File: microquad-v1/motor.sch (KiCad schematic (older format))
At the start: 5 parts, among them M6 Motor_DC, Q6 Q_NMOS_DGS

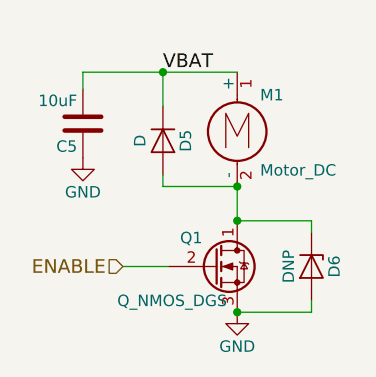
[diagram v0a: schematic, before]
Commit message: Added layout for transistor
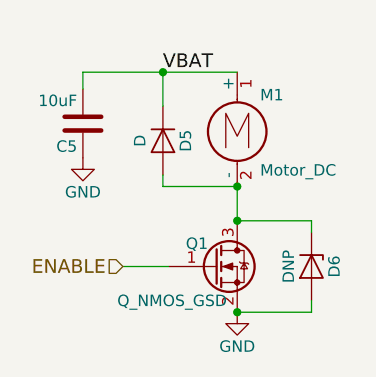
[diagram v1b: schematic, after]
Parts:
- removed Q6: Q_NMOS_DGS, symbol Q_NMOS_DGS
- added Q1: Q_NMOS_GSD, TO_SOT_Packages_SMD:SOT-23, symbol Q_NMOS_GSD
- C10: footprint (none) -> Capacitors_SMD:C_0805
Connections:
- net ENABLE: now also Q1.1 (G)
- net GND: now also Q1.2 (S)
- net at D5.2 (A), D6.1 (K), M6.2 (-): now also Q1.3 (D)
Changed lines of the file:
@@
 $EndDescr
 $Comp
-L Q_NMOS_DGS Q6
-U 1 1 59F7E923
-P 4875 3200
-AR Path="/59F7FFA4/59F7E923" Ref="Q6"  Part="1"
-AR Path="/59F7E793/59F7E923" Ref="Q1"  Part="1"
-AR Path="/59F7F6E8/59F7E923" Ref="Q2"  Part="1"
-AR Path="/59F7FC5E/59F7E923" Ref="Q3"  Part="1"
-AR Path="/59F7FC61/59F7E923" Ref="Q4"  Part="1"
-AR Path="/59F7FFA1/59F7E923" Ref="Q5"  Part="1"
-F 0 "Q1" H 4725 3325 50  0000 L CNN
-F 1 "Q_NMOS_DGS" H 4450 3050 50  0000 L CNN
-F 2 "" H 5075 3300 50  0001 C CNN
-F 3 "" H 4875 3200 50  0001 C CNN
-	1    4875 3200
-	1    0    0    -1
-$EndComp
-$Comp
-L GND #PWR57
+L GND #PWR058
 U 1 1 59F7E92A
 P 4975 3400
-AR Path="/59F7FFA4/59F7E92A" Ref="#PWR57"  Part="1"
-AR Path="/59F7E793/59F7E92A" Ref="#PWR47"  Part="1"
-AR Path="/59F7F6E8/59F7E92A" Ref="#PWR49"  Part="1"
-AR Path="/59F7FC5E/59F7E92A" Ref="#PWR51"  Part="1"
-AR Path="/59F7FC61/59F7E92A" Ref="#PWR53"  Part="1"
-AR Path="/59F7FFA1/59F7E92A" Ref="#PWR55"  Part="1"
-F 0 "#PWR47" H 4975 3150 50  0001 C CNN
+AR Path="/59F7FFA4/59F7E92A" Ref="#PWR058"  Part="1"
+AR Path="/59F7E793/59F7E92A" Ref="#PWR048"  Part="1"
+AR Path="/59F7F6E8/59F7E92A" Ref="#PWR050"  Part="1"
+AR Path="/59F7FC5E/59F7E92A" Ref="#PWR052"  Part="1"
+AR Path="/59F7FC61/59F7E92A" Ref="#PWR054"  Part="1"
+AR Path="/59F7FFA1/59F7E92A" Ref="#PWR056"  Part="1"
+F 0 "#PWR048" H 4975 3150 50  0001 C CNN
 F 1 "GND" H 4975 3250 50  0000 C CNN
 F 2 "" H 4975 3400 50  0001 C CNN
@@
 F 0 "C5" H 4325 2675 50  0000 L CNN
 F 1 "10uF" H 4325 2475 50  0000 L CNN
-F 2 "" H 4338 2425 50  0001 C CNN
+F 2 "Capacitors_SMD:C_0805" H 4338 2425 50  0001 C CNN
 F 3 "" H 4300 2575 50  0001 C CNN
 	1    4300 2575
@@
 Connection ~ 4650 2350
 $Comp
-L GND #PWR56
+L GND #PWR059
 U 1 1 59F80F77
 P 4300 2725
-AR Path="/59F7FFA4/59F80F77" Ref="#PWR56"  Part="1"
-AR Path="/59F7E793/59F80F77" Ref="#PWR46"  Part="1"
-AR Path="/59F7F6E8/59F80F77" Ref="#PWR48"  Part="1"
-AR Path="/59F7FC5E/59F80F77" Ref="#PWR50"  Part="1"
-AR Path="/59F7FC61/59F80F77" Ref="#PWR52"  Part="1"
-AR Path="/59F7FFA1/59F80F77" Ref="#PWR54"  Part="1"
-F 0 "#PWR46" H 4300 2475 50  0001 C CNN
+AR Path="/59F7FFA4/59F80F77" Ref="#PWR059"  Part="1"
+AR Path="/59F7E793/59F80F77" Ref="#PWR049"  Part="1"
+AR Path="/59F7F6E8/59F80F77" Ref="#PWR051"  Part="1"
+AR Path="/59F7FC5E/59F80F77" Ref="#PWR053"  Part="1"
+AR Path="/59F7FC61/59F80F77" Ref="#PWR055"  Part="1"
+AR Path="/59F7FFA1/59F80F77" Ref="#PWR057"  Part="1"
+F 0 "#PWR049" H 4300 2475 50  0001 C CNN
 F 1 "GND" H 4300 2575 50  0000 C CNN
 F 2 "" H 4300 2725 50  0001 C CNN
@@
 Connection ~ 4975 3000
 Connection ~ 4975 3400
+$Comp
+L Q_NMOS_GSD Q1
+U 1 1 59F918D5
+P 4875 3200
+AR Path="/59F7E793/59F918D5" Ref="Q1"  Part="1"
+AR Path="/59F7F6E8/59F918D5" Ref="Q2"  Part="1"
+AR Path="/59F7FC5E/59F918D5" Ref="Q3"  Part="1"
+AR Path="/59F7FC61/59F918D5" Ref="Q4"  Part="1"
+AR Path="/59F7FFA1/59F918D5" Ref="Q5"  Part="1"
+AR Path="/59F7FFA4/59F918D5" Ref="Q6"  Part="1"
+F 0 "Q1" H 4750 3300 50  0000 L CNN
+F 1 "Q_NMOS_GSD" H 4450 3050 50  0000 L CNN
+F 2 "TO_SOT_Packages_SMD:SOT-23" H 5075 3300 50  0001 C CNN
+F 3 "" H 4875 3200 50  0001 C CNN
+	1    4875 3200
+	1    0    0    -1
+$EndComp
 $EndSCHEMATC

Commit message: Finished footprint work 10/31
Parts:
- M6: footprint (none) -> motor:quad_motor_v1
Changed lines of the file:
@@
 AR Path="/59F7FC61/59F7E931" Ref="M4"  Part="1"
 AR Path="/59F7FFA1/59F7E931" Ref="M5"  Part="1"
-F 0 "M1" H 5075 2650 50  0000 L CNN
+F 0 "M6" H 5075 2650 50  0000 L CNN
 F 1 "Motor_DC" H 5075 2350 50  0000 L TNN
-F 2 "" H 4975 2460 50  0001 C CNN
+F 2 "motor:quad_motor_v1" H 4975 2460 50  0001 C CNN
 F 3 "" H 4975 2460 50  0001 C CNN
 	1    4975 2550
@@
 AR Path="/59F7FC61/59F7E93C" Ref="D11"  Part="1"
 AR Path="/59F7FFA1/59F7E93C" Ref="D13"  Part="1"
-F 0 "D5" H 4650 2750 50  0000 C CNN
+F 0 "D15" H 4650 2750 50  0000 C CNN
 F 1 "D" H 4650 2550 50  0000 C CNN
 F 2 "" H 4650 2650 50  0001 C CNN
@@
 AR Path="/59F7FC61/59F7E943" Ref="D12"  Part="1"
 AR Path="/59F7FFA1/59F7E943" Ref="D14"  Part="1"
-F 0 "D6" H 5300 3300 50  0000 C CNN
+F 0 "D16" H 5300 3300 50  0000 C CNN
 F 1 "DNP" H 5300 3100 50  0000 C CNN
 F 2 "" H 5300 3200 50  0001 C CNN
@@
 AR Path="/59F7FC61/59F80E77" Ref="C8"  Part="1"
 AR Path="/59F7FFA1/59F80E77" Ref="C9"  Part="1"
-F 0 "C5" H 4325 2675 50  0000 L CNN
+F 0 "C10" H 4325 2675 50  0000 L CNN
 F 1 "10uF" H 4325 2475 50  0000 L CNN
 F 2 "Capacitors_SMD:C_0805" H 4338 2425 50  0001 C CNN
@@
 AR Path="/59F7FFA1/59F918D5" Ref="Q5"  Part="1"
 AR Path="/59F7FFA4/59F918D5" Ref="Q6"  Part="1"
-F 0 "Q1" H 4750 3300 50  0000 L CNN
+F 0 "Q6" H 4750 3300 50  0000 L CNN
 F 1 "Q_NMOS_GSD" H 4450 3050 50  0000 L CNN
 F 2 "TO_SOT_Packages_SMD:SOT-23" H 5075 3300 50  0001 C CNN

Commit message: Finished in-class work 10/2
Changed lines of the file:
@@
 AR Path="/59F7FC61/59F7E92A" Ref="#PWR054"  Part="1"
 AR Path="/59F7FFA1/59F7E92A" Ref="#PWR056"  Part="1"
-F 0 "#PWR058" H 4975 3150 50  0001 C CNN
+F 0 "#PWR048" H 4975 3150 50  0001 C CNN
 F 1 "GND" H 4975 3250 50  0000 C CNN
 F 2 "" H 4975 3400 50  0001 C CNN
@@
 AR Path="/59F7FC61/59F7E931" Ref="M4"  Part="1"
 AR Path="/59F7FFA1/59F7E931" Ref="M5"  Part="1"
-F 0 "M6" H 5075 2650 50  0000 L CNN
+F 0 "M1" H 5075 2650 50  0000 L CNN
 F 1 "Motor_DC" H 5075 2350 50  0000 L TNN
 F 2 "motor:quad_motor_v1" H 4975 2460 50  0001 C CNN
@@
 AR Path="/59F7FC61/59F7E93C" Ref="D11"  Part="1"
 AR Path="/59F7FFA1/59F7E93C" Ref="D13"  Part="1"
-F 0 "D15" H 4650 2750 50  0000 C CNN
+F 0 "D5" H 4650 2750 50  0000 C CNN
 F 1 "D" H 4650 2550 50  0000 C CNN
 F 2 "" H 4650 2650 50  0001 C CNN
@@
 AR Path="/59F7FC61/59F7E943" Ref="D12"  Part="1"
 AR Path="/59F7FFA1/59F7E943" Ref="D14"  Part="1"
-F 0 "D16" H 5300 3300 50  0000 C CNN
+F 0 "D6" H 5300 3300 50  0000 C CNN
 F 1 "DNP" H 5300 3100 50  0000 C CNN
 F 2 "" H 5300 3200 50  0001 C CNN
@@
 AR Path="/59F7FC61/59F80E77" Ref="C8"  Part="1"
 AR Path="/59F7FFA1/59F80E77" Ref="C9"  Part="1"
-F 0 "C10" H 4325 2675 50  0000 L CNN
+F 0 "C5" H 4325 2675 50  0000 L CNN
 F 1 "10uF" H 4325 2475 50  0000 L CNN
 F 2 "Capacitors_SMD:C_0805" H 4338 2425 50  0001 C CNN
@@
 AR Path="/59F7FC61/59F80F77" Ref="#PWR055"  Part="1"
 AR Path="/59F7FFA1/59F80F77" Ref="#PWR057"  Part="1"
-F 0 "#PWR059" H 4300 2475 50  0001 C CNN
+F 0 "#PWR049" H 4300 2475 50  0001 C CNN
 F 1 "GND" H 4300 2575 50  0000 C CNN
 F 2 "" H 4300 2725 50  0001 C CNN
@@
 AR Path="/59F7FFA1/59F918D5" Ref="Q5"  Part="1"
 AR Path="/59F7FFA4/59F918D5" Ref="Q6"  Part="1"
-F 0 "Q6" H 4750 3300 50  0000 L CNN
+F 0 "Q1" H 4750 3300 50  0000 L CNN
 F 1 "Q_NMOS_GSD" H 4450 3050 50  0000 L CNN
 F 2 "TO_SOT_Packages_SMD:SOT-23" H 5075 3300 50  0001 C CNN

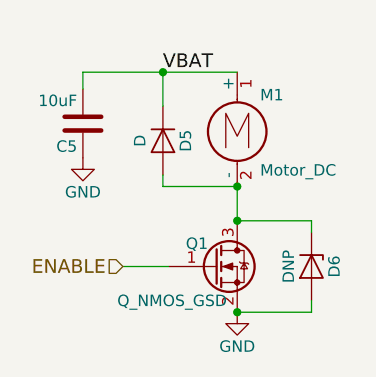
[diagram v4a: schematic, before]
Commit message: Finished footprints for diodes
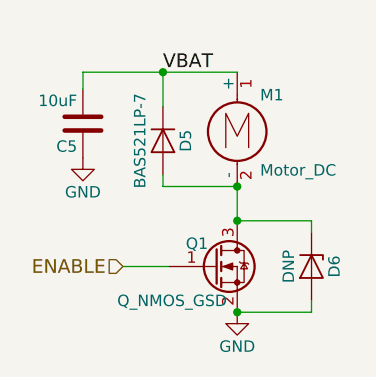
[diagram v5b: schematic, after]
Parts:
- D5: value D -> BAS521LP-7; footprint (none) -> Diodes_SMD:D_SOD-123F
- D6: footprint (none) -> Diodes_SMD:D_2114
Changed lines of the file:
@@
 $EndDescr
 $Comp
-L GND #PWR058
+L GND #PWR057
 U 1 1 59F7E92A
 P 4975 3400
-AR Path="/59F7FFA4/59F7E92A" Ref="#PWR058"  Part="1"
-AR Path="/59F7E793/59F7E92A" Ref="#PWR048"  Part="1"
-AR Path="/59F7F6E8/59F7E92A" Ref="#PWR050"  Part="1"
-AR Path="/59F7FC5E/59F7E92A" Ref="#PWR052"  Part="1"
-AR Path="/59F7FC61/59F7E92A" Ref="#PWR054"  Part="1"
-AR Path="/59F7FFA1/59F7E92A" Ref="#PWR056"  Part="1"
-F 0 "#PWR048" H 4975 3150 50  0001 C CNN
+AR Path="/59F7FFA4/59F7E92A" Ref="#PWR057"  Part="1"
+AR Path="/59F7E793/59F7E92A" Ref="#PWR047"  Part="1"
+AR Path="/59F7F6E8/59F7E92A" Ref="#PWR049"  Part="1"
+AR Path="/59F7FC5E/59F7E92A" Ref="#PWR051"  Part="1"
+AR Path="/59F7FC61/59F7E92A" Ref="#PWR053"  Part="1"
+AR Path="/59F7FFA1/59F7E92A" Ref="#PWR055"  Part="1"
+F 0 "#PWR047" H 4975 3150 50  0001 C CNN
 F 1 "GND" H 4975 3250 50  0000 C CNN
 F 2 "" H 4975 3400 50  0001 C CNN
@@
 AR Path="/59F7FFA1/59F7E93C" Ref="D13"  Part="1"
 F 0 "D5" H 4650 2750 50  0000 C CNN
-F 1 "D" H 4650 2550 50  0000 C CNN
-F 2 "" H 4650 2650 50  0001 C CNN
+F 1 "BAS521LP-7" H 4650 2550 50  0000 C CNN
+F 2 "Diodes_SMD:D_SOD-123F" H 4650 2650 50  0001 C CNN
 F 3 "" H 4650 2650 50  0001 C CNN
 	1    4650 2650
@@
 F 0 "D6" H 5300 3300 50  0000 C CNN
 F 1 "DNP" H 5300 3100 50  0000 C CNN
-F 2 "" H 5300 3200 50  0001 C CNN
+F 2 "Diodes_SMD:D_2114" H 5300 3200 50  0001 C CNN
 F 3 "" H 5300 3200 50  0001 C CNN
 	1    5300 3200
@@
 Connection ~ 4650 2350
 $Comp
-L GND #PWR059
+L GND #PWR058
 U 1 1 59F80F77
 P 4300 2725
-AR Path="/59F7FFA4/59F80F77" Ref="#PWR059"  Part="1"
-AR Path="/59F7E793/59F80F77" Ref="#PWR049"  Part="1"
-AR Path="/59F7F6E8/59F80F77" Ref="#PWR051"  Part="1"
-AR Path="/59F7FC5E/59F80F77" Ref="#PWR053"  Part="1"
-AR Path="/59F7FC61/59F80F77" Ref="#PWR055"  Part="1"
-AR Path="/59F7FFA1/59F80F77" Ref="#PWR057"  Part="1"
-F 0 "#PWR049" H 4300 2475 50  0001 C CNN
+AR Path="/59F7FFA4/59F80F77" Ref="#PWR058"  Part="1"
+AR Path="/59F7E793/59F80F77" Ref="#PWR048"  Part="1"
+AR Path="/59F7F6E8/59F80F77" Ref="#PWR050"  Part="1"
+AR Path="/59F7FC5E/59F80F77" Ref="#PWR052"  Part="1"
+AR Path="/59F7FC61/59F80F77" Ref="#PWR054"  Part="1"
+AR Path="/59F7FFA1/59F80F77" Ref="#PWR056"  Part="1"
+F 0 "#PWR048" H 4300 2475 50  0001 C CNN
 F 1 "GND" H 4300 2575 50  0000 C CNN
 F 2 "" H 4300 2725 50  0001 C CNN

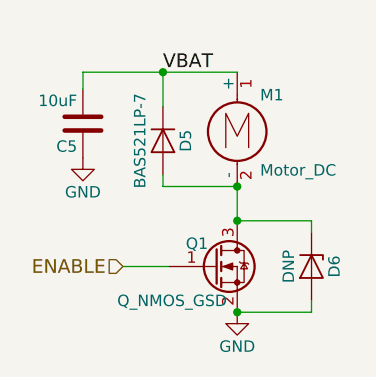
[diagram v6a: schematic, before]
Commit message: Initial power routing to all major chips
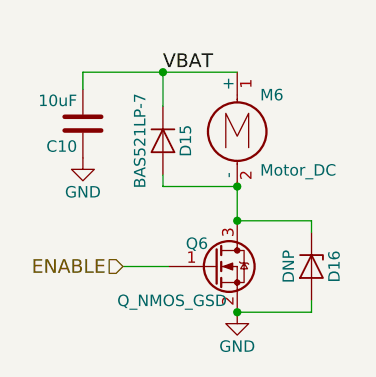
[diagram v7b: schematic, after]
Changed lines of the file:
@@
 AR Path="/59F7FC61/59F7E931" Ref="M4"  Part="1"
 AR Path="/59F7FFA1/59F7E931" Ref="M5"  Part="1"
-F 0 "M1" H 5075 2650 50  0000 L CNN
+F 0 "M6" H 5075 2650 50  0000 L CNN
 F 1 "Motor_DC" H 5075 2350 50  0000 L TNN
 F 2 "motor:quad_motor_v1" H 4975 2460 50  0001 C CNN
@@
 AR Path="/59F7FC61/59F7E93C" Ref="D11"  Part="1"
 AR Path="/59F7FFA1/59F7E93C" Ref="D13"  Part="1"
-F 0 "D5" H 4650 2750 50  0000 C CNN
+F 0 "D15" H 4650 2750 50  0000 C CNN
 F 1 "BAS521LP-7" H 4650 2550 50  0000 C CNN
 F 2 "Diodes_SMD:D_SOD-123F" H 4650 2650 50  0001 C CNN
@@
 AR Path="/59F7FC61/59F7E943" Ref="D12"  Part="1"
 AR Path="/59F7FFA1/59F7E943" Ref="D14"  Part="1"
-F 0 "D6" H 5300 3300 50  0000 C CNN
+F 0 "D16" H 5300 3300 50  0000 C CNN
 F 1 "DNP" H 5300 3100 50  0000 C CNN
 F 2 "Diodes_SMD:D_2114" H 5300 3200 50  0001 C CNN
@@
 AR Path="/59F7FC61/59F80E77" Ref="C8"  Part="1"
 AR Path="/59F7FFA1/59F80E77" Ref="C9"  Part="1"
-F 0 "C5" H 4325 2675 50  0000 L CNN
+F 0 "C10" H 4325 2675 50  0000 L CNN
 F 1 "10uF" H 4325 2475 50  0000 L CNN
 F 2 "Capacitors_SMD:C_0805" H 4338 2425 50  0001 C CNN
@@
 AR Path="/59F7FFA1/59F918D5" Ref="Q5"  Part="1"
 AR Path="/59F7FFA4/59F918D5" Ref="Q6"  Part="1"
-F 0 "Q1" H 4750 3300 50  0000 L CNN
+F 0 "Q6" H 4750 3300 50  0000 L CNN
 F 1 "Q_NMOS_GSD" H 4450 3050 50  0000 L CNN
 F 2 "TO_SOT_Packages_SMD:SOT-23" H 5075 3300 50  0001 C CNN

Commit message: Fixed VBAT connections
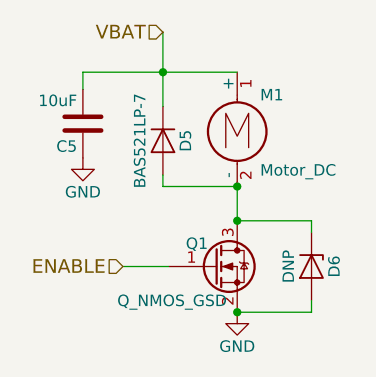
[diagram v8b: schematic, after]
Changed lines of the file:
@@
 AR Path="/59F7FC61/59F7E92A" Ref="#PWR053"  Part="1"
 AR Path="/59F7FFA1/59F7E92A" Ref="#PWR055"  Part="1"
-F 0 "#PWR057" H 4975 3150 50  0001 C CNN
+F 0 "#PWR047" H 4975 3150 50  0001 C CNN
 F 1 "GND" H 4975 3250 50  0000 C CNN
 F 2 "" H 4975 3400 50  0001 C CNN
@@
 	1    0    0    -1
 $EndComp
-Text Label 4650 2350 0    60   ~ 0
-VBAT
 $Comp
 L Motor_DC M6
@@
 AR Path="/59F7FC61/59F7E931" Ref="M4"  Part="1"
 AR Path="/59F7FFA1/59F7E931" Ref="M5"  Part="1"
-F 0 "M6" H 5075 2650 50  0000 L CNN
+F 0 "M1" H 5075 2650 50  0000 L CNN
 F 1 "Motor_DC" H 5075 2350 50  0000 L TNN
 F 2 "motor:quad_motor_v1" H 4975 2460 50  0001 C CNN
@@
 AR Path="/59F7FC61/59F7E93C" Ref="D11"  Part="1"
 AR Path="/59F7FFA1/59F7E93C" Ref="D13"  Part="1"
-F 0 "D15" H 4650 2750 50  0000 C CNN
+F 0 "D5" H 4650 2750 50  0000 C CNN
 F 1 "BAS521LP-7" H 4650 2550 50  0000 C CNN
 F 2 "Diodes_SMD:D_SOD-123F" H 4650 2650 50  0001 C CNN
@@
 AR Path="/59F7FC61/59F7E943" Ref="D12"  Part="1"
 AR Path="/59F7FFA1/59F7E943" Ref="D14"  Part="1"
-F 0 "D16" H 5300 3300 50  0000 C CNN
+F 0 "D6" H 5300 3300 50  0000 C CNN
 F 1 "DNP" H 5300 3100 50  0000 C CNN
 F 2 "Diodes_SMD:D_2114" H 5300 3200 50  0001 C CNN
@@
 	4650 2850 4650 2800
 Wire Wire Line
-	4650 2500 4650 2350
+	4650 2175 4650 2500
 Connection ~ 4975 2850
 $Comp
@@
 AR Path="/59F7FC61/59F80E77" Ref="C8"  Part="1"
 AR Path="/59F7FFA1/59F80E77" Ref="C9"  Part="1"
-F 0 "C10" H 4325 2675 50  0000 L CNN
+F 0 "C5" H 4325 2675 50  0000 L CNN
 F 1 "10uF" H 4325 2475 50  0000 L CNN
 F 2 "Capacitors_SMD:C_0805" H 4338 2425 50  0001 C CNN
@@
 AR Path="/59F7FC61/59F80F77" Ref="#PWR054"  Part="1"
 AR Path="/59F7FFA1/59F80F77" Ref="#PWR056"  Part="1"
-F 0 "#PWR058" H 4300 2475 50  0001 C CNN
+F 0 "#PWR048" H 4300 2475 50  0001 C CNN
 F 1 "GND" H 4300 2575 50  0000 C CNN
 F 2 "" H 4300 2725 50  0001 C CNN
@@
 AR Path="/59F7FFA1/59F918D5" Ref="Q5"  Part="1"
 AR Path="/59F7FFA4/59F918D5" Ref="Q6"  Part="1"
-F 0 "Q6" H 4750 3300 50  0000 L CNN
+F 0 "Q1" H 4750 3300 50  0000 L CNN
 F 1 "Q_NMOS_GSD" H 4450 3050 50  0000 L CNN
 F 2 "TO_SOT_Packages_SMD:SOT-23" H 5075 3300 50  0001 C CNN
@@
 	1    0    0    -1
 $EndComp
+Text HLabel 4650 2175 0    60   Input ~ 0
+VBAT
 $EndSCHEMATC
